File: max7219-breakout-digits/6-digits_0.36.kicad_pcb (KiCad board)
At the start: 2 copper layers, 61.5 x 16 mm, 7 parts, among them J1 Conn_02x08_Odd_Even, U1 HDSM-443B_7-Segment_3_Digit, U2 HDSM-443B_7-Segment_3_Digit

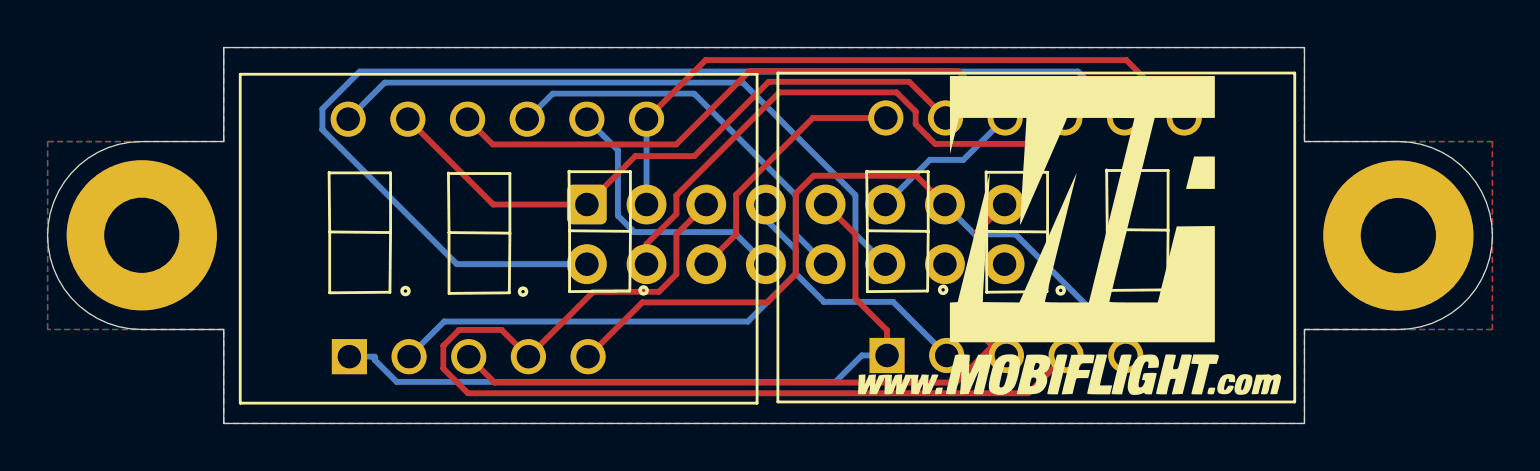
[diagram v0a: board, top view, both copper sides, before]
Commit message: center IDC on all 0.36 display boards
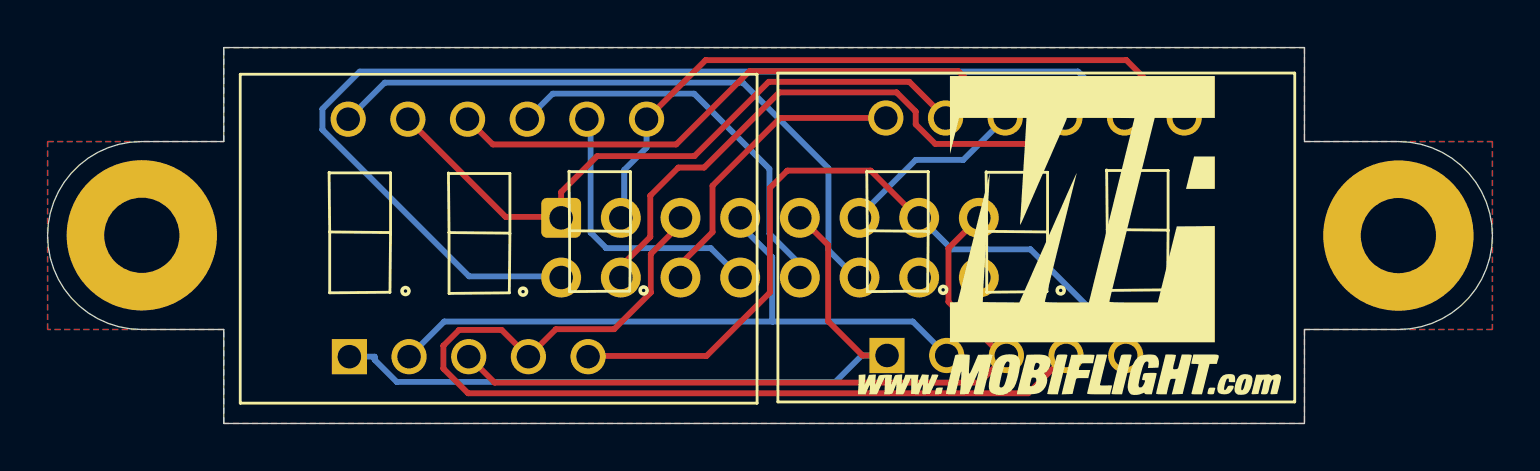
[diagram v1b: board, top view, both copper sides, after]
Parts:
- moved J1 1.23 mm to (105.7, 64.8)
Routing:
- net /F: track 32.1 -> 34.0 mm
- net /DIG1: track 23.5 -> 25.2 mm
- net /B: track 28.6 -> 30.2 mm
- net /G: track 31.5 -> 32.9 mm
- net /DIG2: track 11.2 -> 12.5 mm
- net /C: track 44.2 -> 43.0 mm
- net /A: track 27.2 -> 28.3 mm
- net /DIG0: track 50.1 -> 49.3 mm
- net /DIG5: track 27.7 -> 28.4 mm
- net /DP: track 30.9 -> 31.5 mm
- net /E: track 31.4 -> 31.9 mm
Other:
- board text added: "MobiFlight Display System 6 Digits ${REVISION}"
- board text removed: "6 Digit Module ${REVISION}"

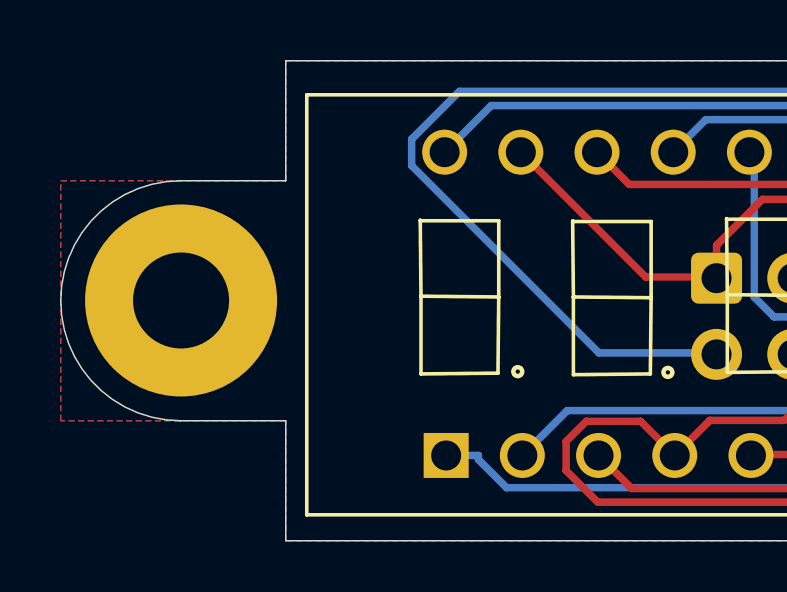
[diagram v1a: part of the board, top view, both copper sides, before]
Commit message: add additional labels on front on backside from all boards
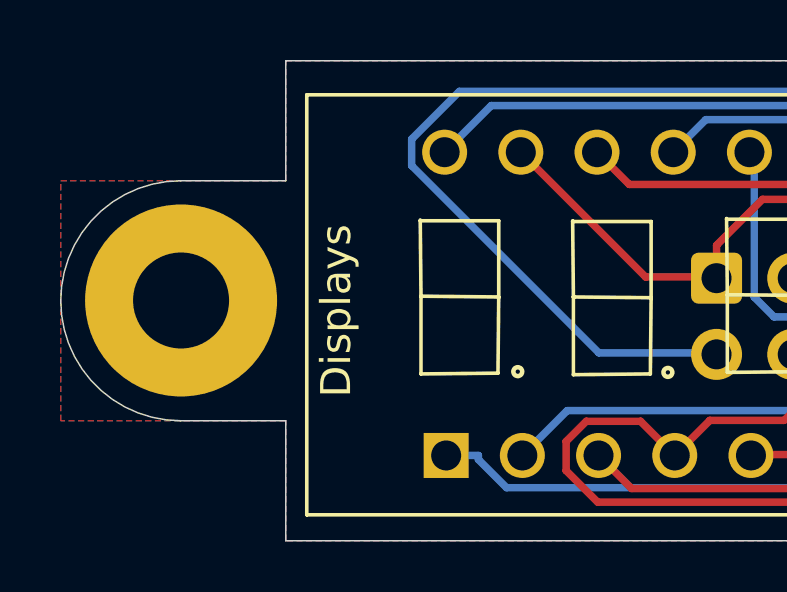
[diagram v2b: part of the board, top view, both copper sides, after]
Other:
- board text added: "Displays"
- board text added: "IDC"
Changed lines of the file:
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@@
 		(tags "Through hole vertical IDC box header THT 2x08 2.54mm double row")
 		(property "Reference" "J1"
-			(at 1.27 6.1 270)
+			(at 1.27 6.1 90)
 			(layer "B.SilkS")
 			(hide yes)
@@
 		)
 		(property "Value" "Conn_02x08_Odd_Even"
-			(at 1.27 -23.88 270)
-			(layer "B.Fab")
+			(at 1.27 -23.88 90)
+			(layer "B.Fab")
+			(hide yes)
 			(effects
 				(font
@@
 		)
 		(property "Datasheet" "~"
-			(at 0 0 270)
+			(at 0 0 90)
 			(layer "F.Fab")
 			(hide yes)
@@
 		)
 		(property "Description" ""
-			(at 0 0 270)
+			(at 0 0 90)
 			(layer "F.Fab")
 			(hide yes)
@@
 		(layer "Edge.Cuts")
 	)
+	(gr_text "Displays"
+		(at 93.64 68.723239 90)
+		(layer "F.SilkS" knockout)
+		(effects
+			(font
+				(size 1 1)
+				(thickness 0.15)
+			)
+			(justify left bottom)
+		)
+	)
 	(gr_text "P.L.+S.H."
 		(at 135.3741 59.003 0)
@@
 		)
 	)
+	(gr_text "IDC"
+		(at 104.531727 63.347293 90)
+		(layer "B.SilkS" knockout)
+		(effects
+			(font
+				(size 2 2)
+				(thickness 0.25)
+			)
+			(justify left bottom mirror)
+		)
+	)

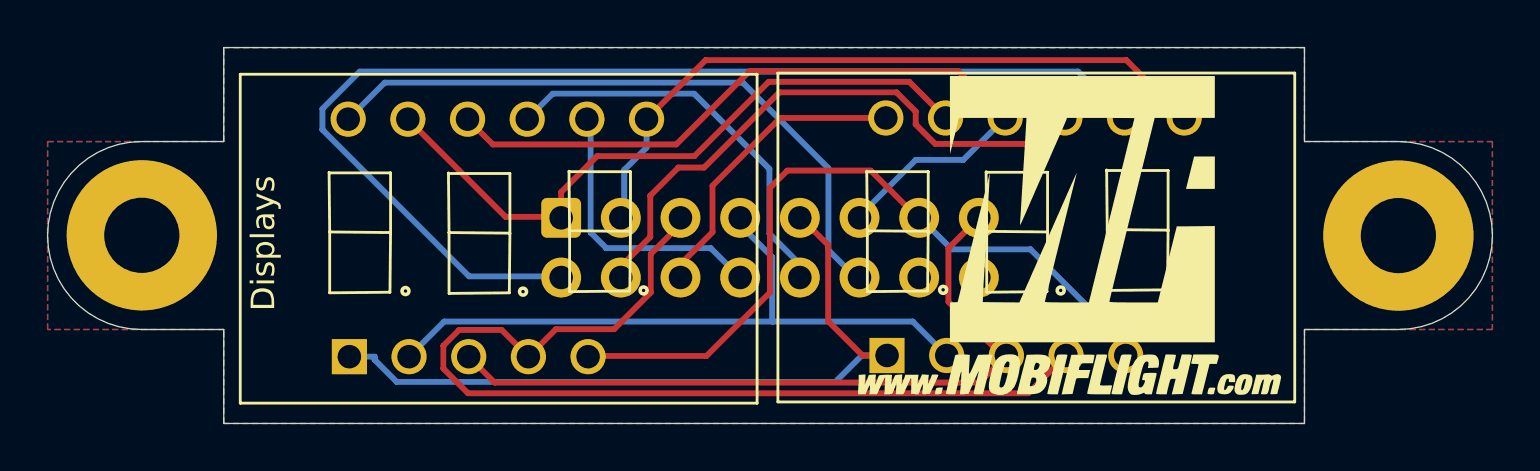
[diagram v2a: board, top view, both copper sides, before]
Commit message: center all IDC connectors on 0.36 boards, move displays closer together
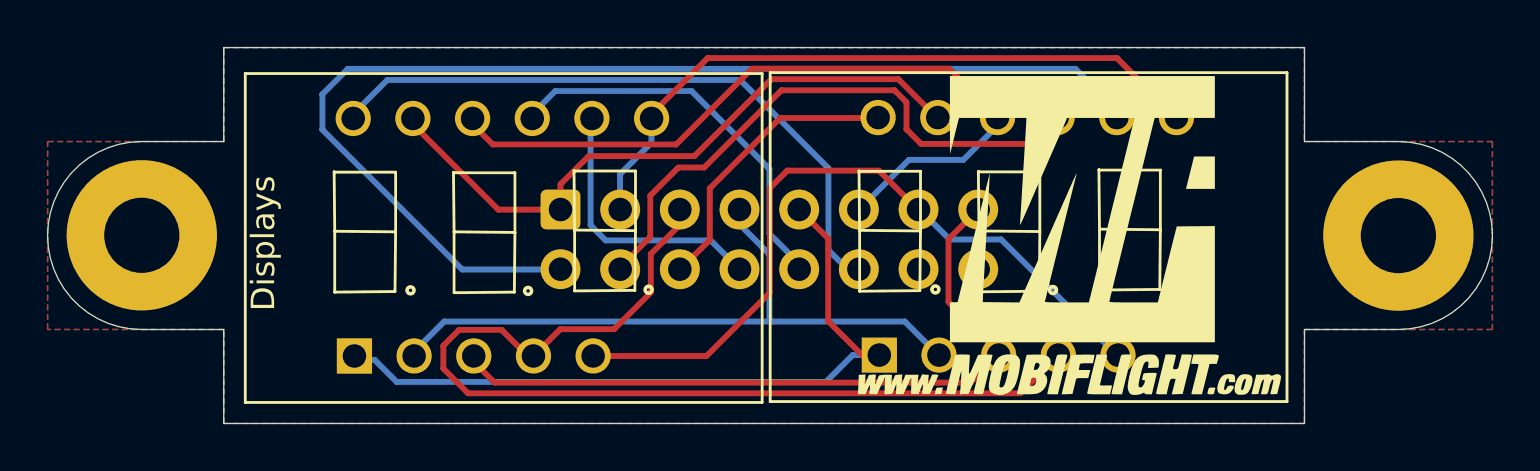
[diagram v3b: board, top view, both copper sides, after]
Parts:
- moved J1 0.35 mm to (105.7, 64.4)
- moved U2 0.33 mm to (127.4, 64.1)
- moved U1 0.22 mm to (105.1, 64.2)
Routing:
- net /B: track 30.2 -> 29.0 mm
- net /F: track 34.0 -> 33.0 mm
- net /G: track 32.9 -> 32.1 mm
- net /A: track 28.3 -> 27.8 mm
